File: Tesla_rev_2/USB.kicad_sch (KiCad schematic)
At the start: 16 parts, among them J10 USB_C_Receptacle_USB2.0_16P, Q1 BC817, Q2 BC817, SW1 SW_Push, U2 USBLC6-2P6, U3 CH340C

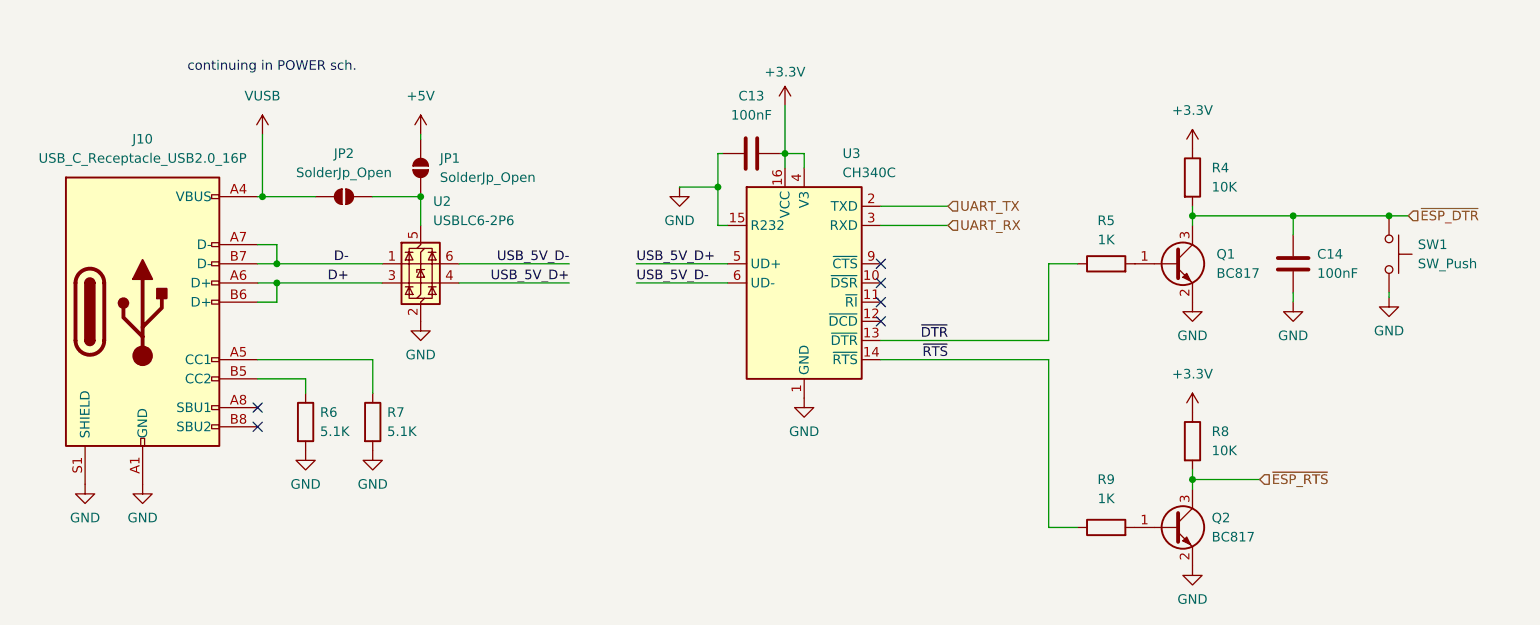
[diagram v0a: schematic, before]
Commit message: Netclasses, part Nums, LPF adjust
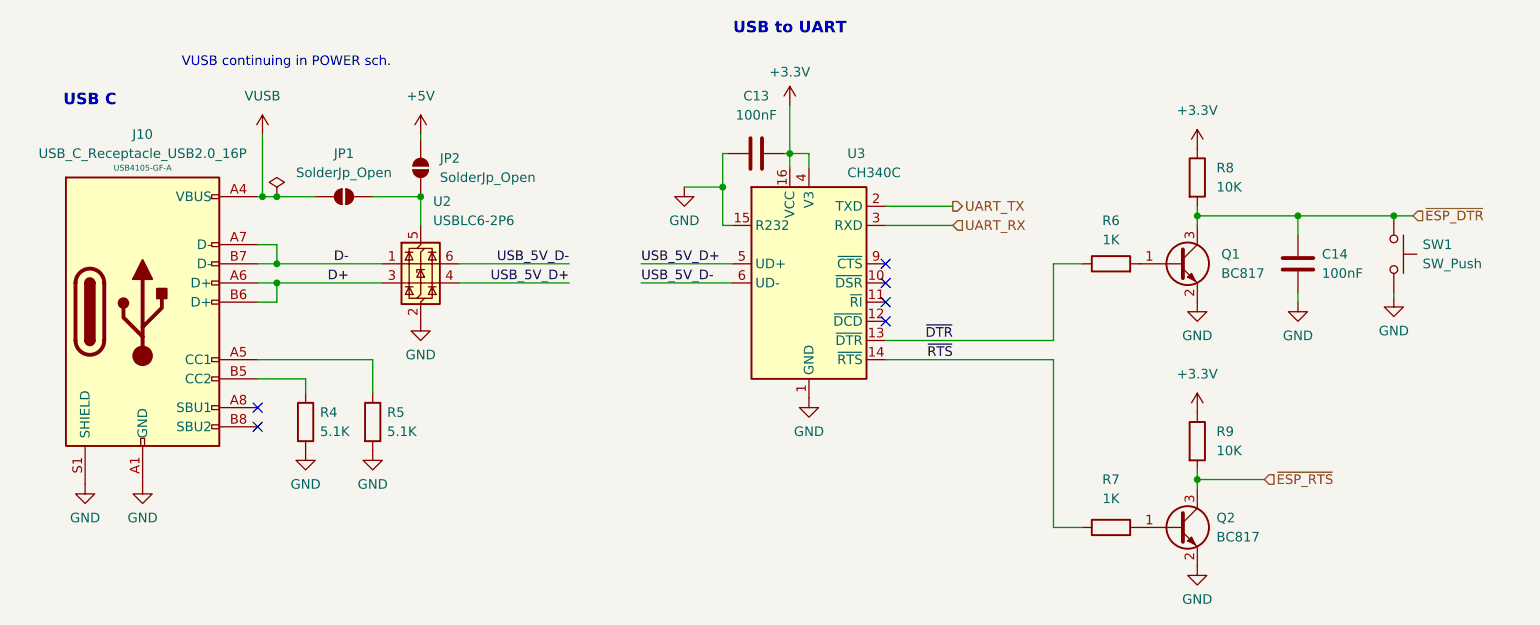
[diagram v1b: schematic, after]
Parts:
- J10: Part_num (none) -> USB4105-GF-A
- renumbered JP2 to JP1, JP1 to JP2, R6 to R4, R7 to R5, R5 to R6, R9 to R7, R4 to R8, R8 to R9
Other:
- note added: "USB C"
- note added: "USB to UART"
- note added: "VUSB continuing in POWER sch."
- note removed: "continuing in POWER sch."
- title: (none) -> Tesla sextant BT
- moved on the sheet: C13, C14, Q1, Q2, R6, R7, R8, R9, SW1, U3
